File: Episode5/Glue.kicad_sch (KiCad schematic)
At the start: 15 parts, among them U5 ATF750CL, U6 ATF22V10C, U7 ATF750CL, U8 ATF750CL

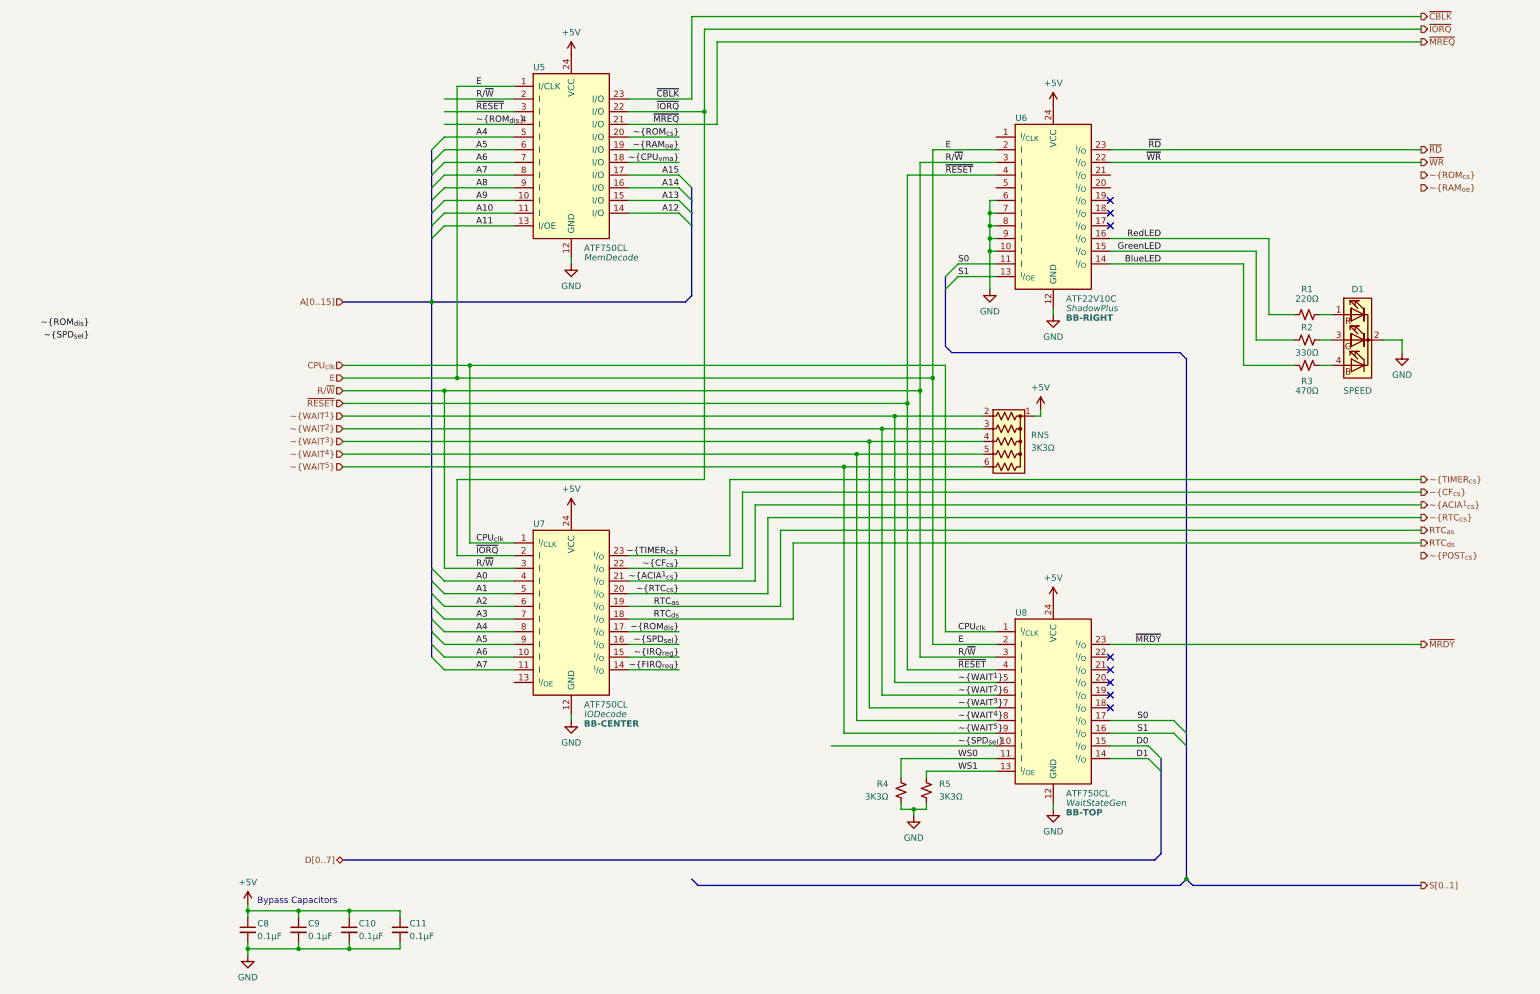
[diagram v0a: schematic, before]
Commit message: Placed Global labels instead. And toying with new PLDs
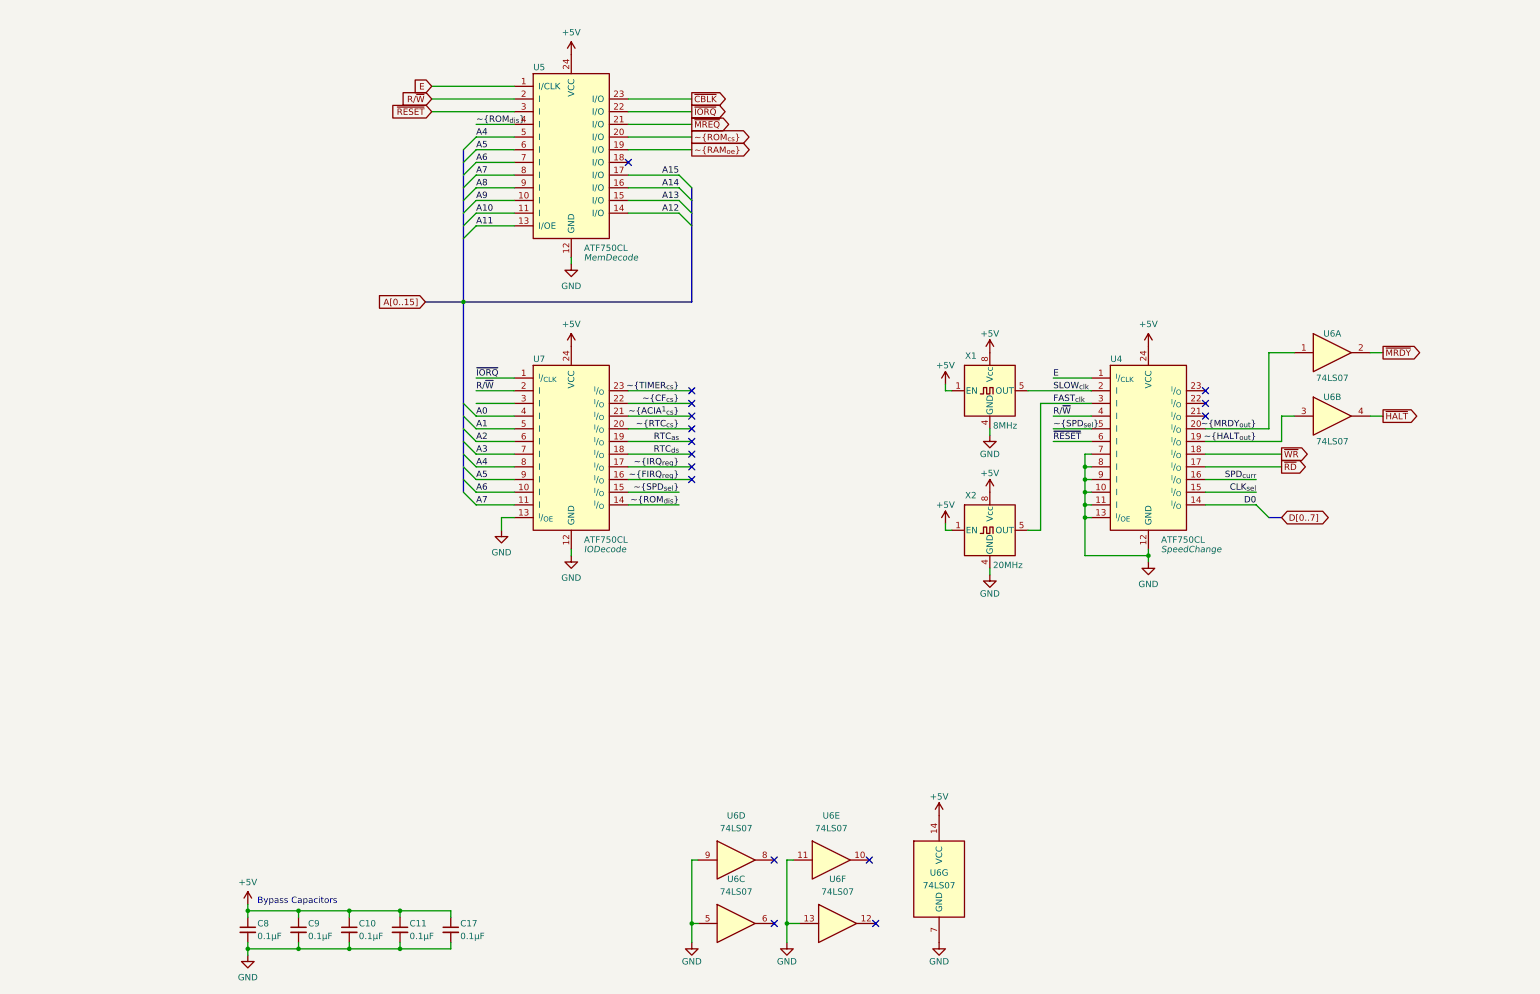
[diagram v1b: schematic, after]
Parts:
- removed D1: SPEED, symbol Device:LED_RKGB
- removed R1: 220Ω, symbol Device:R_Small_US
- removed R2: 330Ω, symbol Device:R_Small_US
- removed R3: 470Ω, symbol Device:R_Small_US
- removed R4, R5: 3K3Ω, symbol Device:R_Small_US
- removed RN5: 3K3Ω, Resistor_THT:R_Array_SIP6, symbol Device:R_Network05_US
- removed U6: ATF22V10C, Package_DIP:DIP-24_W7.62mm_Socket_LongPads, symbol MicroHobbyist:ATF750C
- removed U8: ATF750CL, Package_DIP:DIP-24_W7.62mm_Socket_LongPads, symbol MicroHobbyist:ATF750C
- added C17: 0.1µF, symbol Device:C_Small
- added U4: ATF750CL, Package_DIP:DIP-24_W7.62mm_Socket_LongPads, symbol MicroHobbyist:ATF750C
- added U6: 74LS07, symbol 74xx:74LS07
- added X1: 8MHz, Oscillator:Oscillator_DIP-8, symbol Oscillator:CXO_DIP8
- added X2: 20MHz, Oscillator:Oscillator_DIP-8, symbol Oscillator:CXO_DIP8
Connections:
- net CPU_{clk} is gone; now on net ~{IORQ}: U7.1 (^{I}/_{CLK})
- net +5V: now also C17.1, U4.24 (VCC), U6.14 (VCC), X1.1 (EN), X1.8 (Vcc), X2.1 (EN), X2.8 (Vcc)
- net D0: now also U4.14 (^{I}/_{O})
- net E: now also U4.1 (^{I}/_{CLK})
- net GND: now also U7.13 (^{I}/_{OE}), C17.2, U4.10 (I), U4.11 (I), U4.12 (GND), U4.13 (^{I}/_{OE}), U4.7 (I), U4.8 (I), U4.9 (I), U6.11, U6.13, U6.5, U6.7 (GND), U6.9, X1.4 (GND), X2.4 (GND)
- net R/~{W}: now also U7.2 (I), U4.4 (I); no longer U7.3 (I)
- net ~{FIRQ_{reg}}: now also U7.16 (^{I}/_{O}); no longer U7.14 (^{I}/_{O})
- net ~{IORQ}: no longer U7.2 (I)
- net ~{IRQ_{reg}}: now also U7.17 (^{I}/_{O}); no longer U7.15 (^{I}/_{O})
- net ~{MRDY}: now also U6.2
- net ~{RD}: now also U4.17 (^{I}/_{O})
- net ~{RESET}: now also U4.6 (I)
- net ~{ROM_{dis}}: now also U7.14 (^{I}/_{O}); no longer U7.17 (^{I}/_{O})
- net ~{SPD_{sel}}: now also U7.15 (^{I}/_{O}), U4.5 (I); no longer U7.16 (^{I}/_{O})
- net ~{WR}: now also U4.18 (^{I}/_{O})
- net ~{CPU_{vma}}: no longer names the net of U5.18 (I/O)
- new net CLK_{sel}: U4.15 (^{I}/_{O})
- new net FAST_{clk}: U4.3 (I), X2.5 (OUT)
- new net SLOW_{clk}: U4.2 (I), X1.5 (OUT)
- new net SPD_{curr}: U4.16 (^{I}/_{O})
- new net ~{HALT_{out}}: U4.19 (^{I}/_{O}), U6.3
- new net ~{HALT}: U6.4
- new net ~{MRDY_{out}}: U4.20 (^{I}/_{O}), U6.1
- no-connect marks 8 -> 16
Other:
- moved on the sheet: U7

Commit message: Toying with different alternatives for the CPU board
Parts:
- removed U4: ATF750CL, Package_DIP:DIP-24_W7.62mm_Socket_LongPads, symbol MicroHobbyist:ATF750C
- removed unit 3 of U6
- removed unit 6 of U6
- removed unit 4 of U6
- removed unit 7 of U6
- removed unit 2 of U6
- removed unit 5 of U6
- removed X1: 8MHz, Oscillator:Oscillator_DIP-8, symbol Oscillator:CXO_DIP8
- removed X2: 20MHz, Oscillator:Oscillator_DIP-8, symbol Oscillator:CXO_DIP8
- added U10, U12: ATF750CL, Package_DIP:DIP-24_W7.62mm_Socket_LongPads, symbol MicroHobbyist:ATF22V10C
- renumbered C8 to C13, C9 to C14, C10 to C15, C11 to C16, U7 to U11, U6 to U13, U5 to U9
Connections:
- net ~{CF_{cs}} is gone; now on net ~{TIMER_{cs}}: U11.22 (^{I}/_{O})
- net ~{SPD_{sel}} is gone; now on net ~{WR}: U11.15 (^{I}/_{O})
- net +5V: now also U10.24 (VCC), U12.24 (VCC)
- net A0: now also U11.5 (I), U10.14 (I/O), U12.14 (I/O); no longer U11.4 (I)
- net A1: now also U11.6 (I); no longer U11.5 (I)
- net A2: now also U11.7 (I); no longer U11.6 (I)
- net A3: now also U11.8 (I); no longer U11.7 (I)
- net A4: now also U11.9 (I); no longer U11.8 (I)
- net A5: now also U11.10 (I); no longer U11.9 (I)
- net A6: now also U11.11 (I); no longer U11.10 (I)
- net A7: now also U11.13 (^{I}/_{OE}); no longer U11.11 (I)
- net D0: now also U10.23 (I/O), U12.23 (I/O)
- net E: now also U11.4 (I), U10.1 (I/CLK), U12.1 (I/CLK)
- net GND: now also U10.12 (GND), U12.10 (I), U12.11 (I), U12.12 (GND), U12.13 (I/OE), U12.9 (I); no longer U11.13 (^{I}/_{OE})
- net RTC_{as}: now also U11.20 (^{I}/_{O}); no longer U11.19 (^{I}/_{O})
- net RTC_{ds}: now also U11.19 (^{I}/_{O}); no longer U11.18 (^{I}/_{O})
- net R/~{W}: now also U11.3 (I), U10.3 (I), U12.3 (I); no longer U11.2 (I)
- net ~{ACIA^{1}_{cs}}: now also U11.23 (^{I}/_{O}); no longer U11.21 (^{I}/_{O})
- net ~{FIRQ_{reg}}: now also U12.2 (I)
- net ~{IORQ}: now also U11.2 (I); no longer U11.1 (^{I}/_{CLK})
- net ~{IRQ_{reg}}: now also U10.2 (I)
- net ~{RD}: now also U9.18 (I/O)
- net ~{RESET}: now also U10.4 (I), U12.4 (I)
- net ~{ROM_{dis}}: now also U11.18 (^{I}/_{O}); no longer U11.14 (^{I}/_{O})
- net ~{RTC_{cs}}: now also U11.21 (^{I}/_{O}); no longer U11.20 (^{I}/_{O})
- net ~{TIMER_{cs}}: no longer U11.23 (^{I}/_{O})
- net ~{MRDY_{out}}: no longer names the net of U13.1
- net ~{MRDY_{out}}: now also U11.14 (^{I}/_{O})
- new net CPU_{clk}: U11.1 (^{I}/_{CLK})
- new net D1: U10.22 (I/O), U12.22 (I/O)
- new net D2: U10.21 (I/O), U12.21 (I/O)
- new net D3: U10.20 (I/O), U12.20 (I/O)
- new net D4: U10.19 (I/O), U12.19 (I/O)
- new net D5: U10.18 (I/O), U12.18 (I/O)
- new net D6: U10.17 (I/O), U12.17 (I/O)
- new net D7: U10.16 (I/O), U12.16 (I/O)
- new net ~{FIRQ}: U12.15 (I/O)
- new net ~{FIRQ}0: U12.5 (I)
- new net ~{FIRQ}1: U12.6 (I)
- new net ~{FIRQ}2: U12.7 (I)
- new net ~{FIRQ}3: U12.8 (I)
- new net ~{IRQ}: U10.15 (I/O)
- new net ~{IRQ}0: U10.5 (I)
- new net ~{IRQ}1: U10.6 (I)
- new net ~{IRQ}2: U10.7 (I)
- new net ~{IRQ}3: U10.8 (I)
- new net ~{IRQ}4: U10.9 (I)
- new net ~{IRQ}5: U10.10 (I)
- new net ~{IRQ}6: U10.11 (I)
- new net ~{IRQ}7: U10.13 (I/OE)
- no-connect marks 16 -> 0
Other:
- moved on the sheet: U11, U13A, U9

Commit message: Finished the preliminary design of the CPU card
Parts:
- removed U10, U12: ATF750CL, Package_DIP:DIP-24_W7.62mm_Socket_LongPads, symbol MicroHobbyist:ATF22V10C
- added C14, C15, C16, C17: 0.1µF, symbol Device:C_Small
- added C8: 1µF, Capacitor_THT:C_Disc_D3.0mm_W1.6mm_P2.50mm, symbol Device:C
- added LED1: SPEED, PCM_LED_THT_AKL:LED_Rectangular_W5.0mm_H2.0mm-CC, symbol PCM_LED_AKL:LED_2x5mm_Kcom_Green_Red
- added R14: 220Ω, symbol Device:R_Small_US
- added R15: 330Ω, symbol Device:R_Small_US
- added R16: 1KΩ, Resistor_THT:R_Axial_DIN0207_L6.3mm_D2.5mm_P10.16mm_Horizontal, symbol Device:R_US
- added R17: 4k7Ω, symbol Device:R_Small_US
- added R18: 20KΩ, Resistor_THT:R_Axial_DIN0207_L6.3mm_D2.5mm_P10.16mm_Horizontal, symbol Device:R_US
- added SW2: SPEED, symbol Switch:SW_Push
- added U11: ATF22V10C, Package_DIP:DIP-24_W7.62mm_Socket_LongPads, symbol MicroHobbyist:ATF22V10C
- added U12: 74AHCT14, symbol 74xx:74HC14
- added U8: ATF750CL, Package_DIP:DIP-24_W7.62mm_Socket_LongPads, symbol MicroHobbyist:ATF22V10C
- added unit 2 of U9
- added unit 3 of U9
- added X1: 20MHz, Oscillator:Oscillator_DIP-8, symbol Oscillator:CXO_DIP8
- added X2: 8MHz, Oscillator:Oscillator_DIP-8, symbol Oscillator:CXO_DIP8
- U7: renamed from U9; value ATF750CL -> ATF22V10C
- U9: renamed from U13; value 74LS07 -> 74AHCT07
- renumbered C14 to C10, C15 to C11, C16 to C12, C17 to C13, C13 to C9, U11 to U10
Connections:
- net +5V: now also C14.1, C15.1, C16.1, C17.1, R16.1, R17.2, U11.24 (VCC), U8.24 (VCC), X1.1 (EN), X1.8 (Vcc), X2.1 (EN), X2.8 (Vcc)
- net A0: now also U7.2 (I)
- net A1: now also U7.3 (I)
- net A10: now also U7.13 (I/OE); no longer U7.11 (I)
- net A11: now also U7.17 (I/O); no longer U7.13 (I/OE)
- net A12: now also U7.16 (I/O); no longer U7.14 (I/O)
- net A14: now also U7.14 (I/O); no longer U7.16 (I/O)
- net A15: now also U7.18 (I/O); no longer U7.17 (I/O)
- net A2: now also U7.4 (I)
- net A3: now also U7.5 (I)
- net A4: now also U7.6 (I); no longer U7.5 (I)
- net A5: now also U7.7 (I); no longer U7.6 (I)
- net A6: now also U7.8 (I); no longer U7.7 (I)
- net A7: now also U7.9 (I); no longer U7.8 (I)
- net A8: now also U7.10 (I); no longer U7.9 (I)
- net A9: now also U7.11 (I); no longer U7.10 (I)
- net D0: now also U8.20 (I/O)
- net E: now also U8.1 (I/CLK); no longer U10.4 (I)
- net GND: now also U10.4 (I), C14.2, C15.2, C16.2, C17.2, C8.2, LED1.2 (K), SW2.1, U11.10 (I), U11.11 (I), U11.12 (GND), U11.13 (I/OE), U11.5 (I), U11.6 (I), U11.7 (I), U11.8 (I), U11.9 (I), U8.10 (I), U8.11 (I), U8.12 (GND), U8.13 (I/OE), U8.8 (I), U8.9 (I), X1.4 (GND), X2.4 (GND)
- net R/~{W}: now also U11.3 (I), U8.4 (I); no longer U7.2 (I)
- net ~{FIRQ_{reg}}: now also U7.19 (I/O); no longer U10.16 (^{I}/_{O})
- net ~{IRQ_{reg}}: now also U7.20 (I/O); no longer U10.17 (^{I}/_{O})
- net ~{MRDY}: now also U9.6
- net ~{RAM_{oe}}: now also U11.21 (I/O); no longer U7.19 (I/O)
- net ~{RD}: now also U11.20 (I/O); no longer U7.18 (I/O)
- net ~{RESET}: now also U11.4 (I), U8.6 (I); no longer U7.3 (I)
- net ~{ROM_{cs}}: now also U11.23 (I/O); no longer U7.20 (I/O)
- net ~{ROM_{dis}}: now also U10.16 (^{I}/_{O}), U11.1 (I/CLK); no longer U10.18 (^{I}/_{O}), U7.4 (I)
- net ~{WR}: now also U11.19 (I/O); no longer U10.15 (^{I}/_{O})
- net CPU_{clk} renamed CLK_{slow}
- net CLK_{slow}: now also U8.2 (I), X1.5 (OUT)
- new net: R16.2, R18.1, SW2.2
- new net: U8.14 (I/O), U9.5
- new net: U8.15 (I/O), U9.3
- new net: LED1.3 (A2), R15.1
- new net: C8.1, R18.2, U12.1
- new net: LED1.1 (A1), R14.1
- new net CLK_{cpu}: U8.23 (I/O)
- new net CLK_{fast}: U8.3 (I), X2.5 (OUT)
- new net SPD_{btn}: U12.2, U8.7 (I)
- new net SPD_{cpu}: R15.2, U8.22 (I/O)
- new net ~{CART_{cs}}: U11.22 (I/O)
- new net ~{CART_{det}}: R17.1, U11.2 (I)
- new net ~{CONF_{cs}}: U10.17 (^{I}/_{O})
- new net ~{HALT}: U9.4
- new net ~{POST_{cs}}: U10.18 (^{I}/_{O})
- new net ~{SPD_{cpu}}: R14.2, U8.21 (I/O)
- new net ~{SPD_{sel}}: U10.15 (^{I}/_{O}), U8.5 (I)
- no-connect marks 0 -> 9
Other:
- company: Frédéric "MicroHobbyist" Segard -> MicroHobbyist
- title: (none) -> Glue Logic and Interrupt Controllers
- moved on the sheet: U10, U7, U9A
